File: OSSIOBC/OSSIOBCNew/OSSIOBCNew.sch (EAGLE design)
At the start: 151 parts, among them Q2 NX-3215, U1 PCA9548APWR, U10 MAX6369, U11 OPA4347, U12 TPS73233, U13 SN65HVD11QD, U14 LTC4411, U16 DS3231-L, U17 FM24V02-G, U18 TMP101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

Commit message: New OBC schematic / board file ok
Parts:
- removed C35: 1uF 0805, OSSI:C0805(2012)
- removed U12: TPS73233, OSSI:TPS73233
- added C42: 10uF, LDO Tantal 16V, OSSI:C-TANTAL-A
- added R75, R76, R77: 0, OSSI:R0603(1608)
- added U$1: OSSILOGORECT, OSSI:OSSILOGORECT
- added U15: MCP1700_SOT23, OSSI:MCP1700_SOT23
- C34: value 1uF 0805 -> 10uF, LDO Tantal 16V; device OSSI:C0805(2012) -> OSSI:C-TANTAL-A
- U9: value ADR127BUJZ-REEL7 -> ADR121
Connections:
- new net N$59: C42.-, R75.1
- new net N$62: R76.1, U5.49
- new net N$64: R77.1, U5.50
- net 3.3VOBC: now also C42.+, U15.2; no longer C34.1, R5.2, R72.2, U12.5
- net 3.3VOBC_I2C: now also R5.2, R72.2
- net GND: now also C34.-, R75.2, U15.1; no longer C34.2, C35.2, U12.2
- net MUX_A0: now also R76.2; no longer U5.49
- net MUX_A1: now also R77.2; no longer U5.50
- net N$666: now also C34.+, U15.3; no longer C35.1, U12.1, U12.3
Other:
- note added: "Remove 0 Ohm for SMCLK / ACLK out"
- moved on the sheet: C5

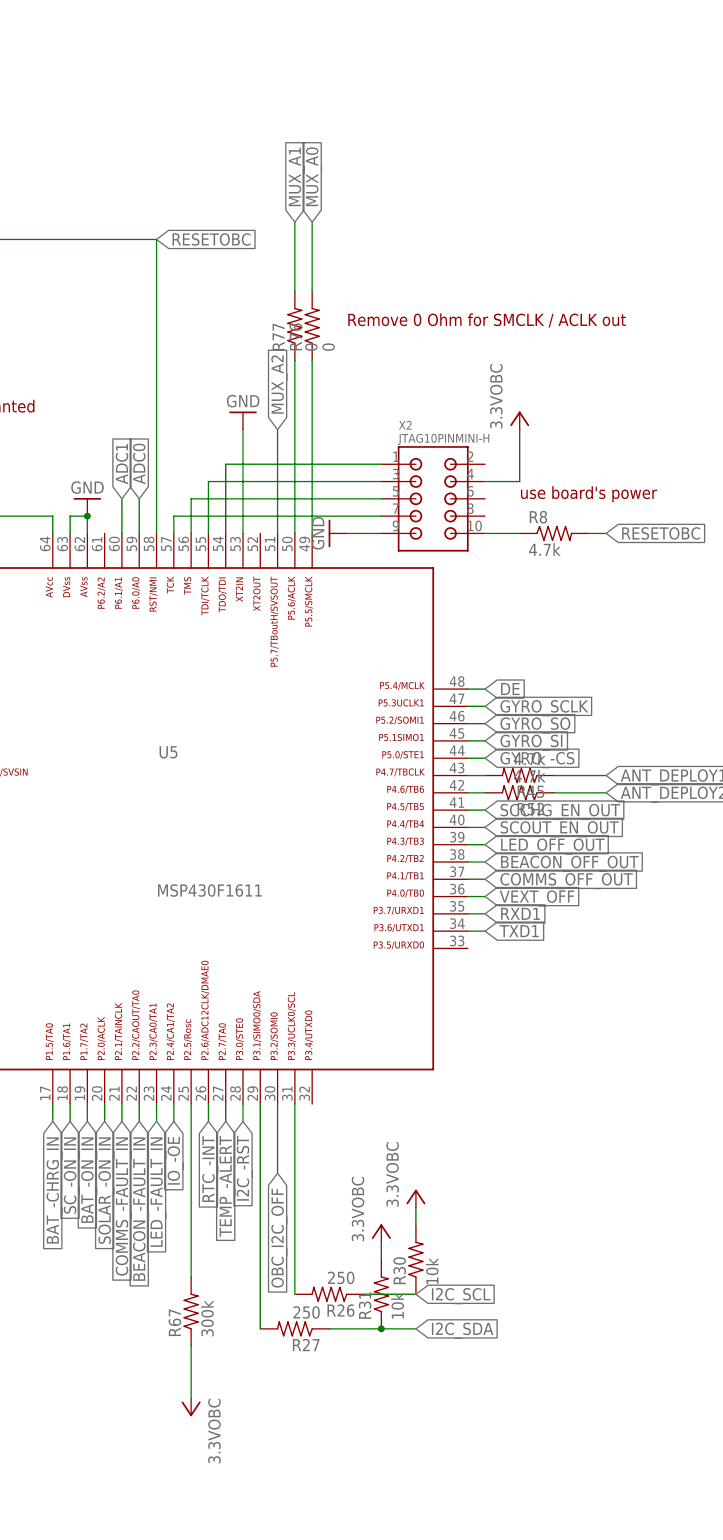
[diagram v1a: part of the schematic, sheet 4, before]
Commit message: OSSI OBC New Gerber file added
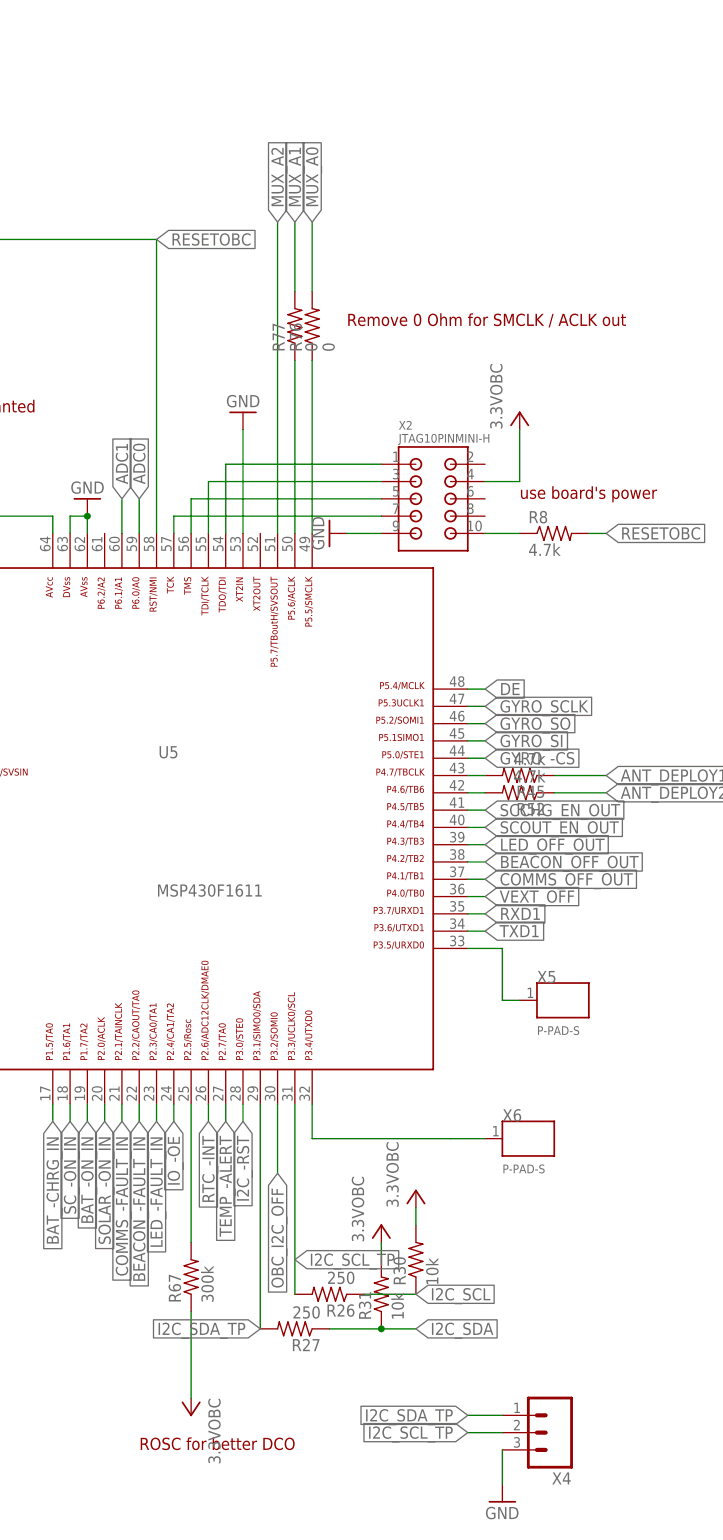
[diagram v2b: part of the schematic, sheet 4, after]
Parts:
- added X4: (no value), OSSI:M03PTH
- added X5, X6: P-PAD-S, OSSI:P-PAD-S
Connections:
- new net I2C_SCL_TP: R26.2, U5.31, X4.2
- new net I2C_SDA_TP: R27.2, U5.29, X4.1
- net GND: now also X4.3
- net N$60: now also U5.33, X5.P$1; no longer R27.2, U5.29
- net N$61: now also U5.32, X6.P$1; no longer R26.2, U5.31
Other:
- note added: "ROSC for better DCO"
- moved on the sheet: R67
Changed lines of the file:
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@@
 <part name="R76" library="OSSI" deviceset="R" device="0603(1608)" value="0"/>
 <part name="R77" library="OSSI" deviceset="R" device="0603(1608)" value="0"/>
+<part name="X4" library="OSSI" deviceset="M03" device="PTH"/>
+<part name="GND81" library="OSSI" deviceset="GND" device=""/>
+<part name="X5" library="OSSI" deviceset="P-PAD" device="-S"/>
+<part name="X6" library="OSSI" deviceset="P-PAD" device="-S"/>
 </parts>
 <sheets>
@@
 <text x="121.92" y="114.3" size="1.778" layer="94">led</text>
 <text x="238.76" y="205.74" size="1.778" layer="94">Remove 0 Ohm for SMCLK / ACLK out</text>
+<text x="208.28" y="40.64" size="1.778" layer="94">ROSC for better DCO</text>
 </plain>
 <instances>
@@
 <instance part="GND74" gate="1" x="114.3" y="88.9"/>
 <instance part="GND70" gate="1" x="223.52" y="193.04" rot="R180"/>
-<instance part="R67" gate="G$1" x="215.9" y="60.96" rot="R90"/>
+<instance part="R67" gate="G$1" x="215.9" y="66.04" rot="R90"/>
 <instance part="3.3VOBC16" gate="G$1" x="215.9" y="48.26" rot="R180"/>
 <instance part="JP1" gate="A" x="129.54" y="99.06"/>
@@
 <instance part="R76" gate="G$1" x="233.68" y="205.74" rot="R90"/>
 <instance part="R77" gate="G$1" x="231.14" y="205.74" rot="R90"/>
+<instance part="X4" gate="G$1" x="269.24" y="43.18" rot="R180"/>
+<instance part="GND81" gate="1" x="261.62" y="33.02"/>
+<instance part="X5" gate="G$1" x="269.24" y="106.68"/>
+<instance part="X6" gate="G$1" x="264.16" y="86.36"/>
 </instances>
 <busses>
@@
 <wire x1="142.24" y1="220.98" x2="142.24" y2="223.52" width="0.1524" layer="91"/>
 </segment>
+<segment>
+<pinref part="X4" gate="G$1" pin="3"/>
+<pinref part="GND81" gate="1" pin="GND"/>
+<wire x1="261.62" y1="40.64" x2="261.62" y2="35.56" width="0.1524" layer="91"/>
+</segment>
 </net>
 <net name="RESETOBC" class="0">
@@
 </segment>
 </net>
-<net name="N$60" class="0">
+<net name="I2C_SDA_TP" class="0">
 <segment>
 <pinref part="U5" gate="G$1" pin="29"/>
 <wire x1="226.06" y1="91.44" x2="226.06" y2="58.42" width="0.1524" layer="91"/>
 <pinref part="R27" gate="G$1" pin="2"/>
+<label x="226.06" y="58.42" size="1.778" layer="95" rot="R180" xref="yes"/>
+</segment>
+<segment>
+<pinref part="X4" gate="G$1" pin="1"/>
+<wire x1="261.62" y1="45.72" x2="256.54" y2="45.72" width="0.1524" layer="91"/>
+<label x="256.54" y="45.72" size="1.778" layer="95" rot="R180" xref="yes"/>
 </segment>
 </net>
-<net name="N$61" class="0">
+<net name="I2C_SCL_TP" class="0">
 <segment>
 <pinref part="U5" gate="G$1" pin="31"/>
 <wire x1="231.14" y1="91.44" x2="231.14" y2="63.5" width="0.1524" layer="91"/>
 <pinref part="R26" gate="G$1" pin="2"/>
+<label x="231.14" y="68.58" size="1.778" layer="95" xref="yes"/>
+</segment>
+<segment>
+<pinref part="X4" gate="G$1" pin="2"/>
+<wire x1="261.62" y1="43.18" x2="256.54" y2="43.18" width="0.1524" layer="91"/>
+<label x="256.54" y="43.18" size="1.778" layer="95" rot="R180" xref="yes"/>
 </segment>
 </net>
@@
 <pinref part="3.3VOBC16" gate="G$1" pin="3.3VOBC"/>
 <pinref part="R67" gate="G$1" pin="1"/>
-<wire x1="215.9" y1="48.26" x2="215.9" y2="55.88" width="0.1524" layer="91"/>
+<wire x1="215.9" y1="48.26" x2="215.9" y2="60.96" width="0.1524" layer="91"/>
 </segment>
 </net>
@@
 <segment>
 <pinref part="U5" gate="G$1" pin="51"/>
-<wire x1="228.6" y1="175.26" x2="228.6" y2="190.5" width="0.1524" layer="91"/>
-<label x="228.6" y="190.5" size="1.778" layer="95" rot="R90" xref="yes"/>
+<wire x1="228.6" y1="175.26" x2="228.6" y2="220.98" width="0.1524" layer="91"/>
+<label x="228.6" y="220.98" size="1.778" layer="95" rot="R90" xref="yes"/>
 </segment>
 </net>
@@
 <pinref part="R67" gate="G$1" pin="2"/>
 <pinref part="U5" gate="G$1" pin="25"/>
-<wire x1="215.9" y1="66.04" x2="215.9" y2="91.44" width="0.1524" layer="91"/>
+<wire x1="215.9" y1="71.12" x2="215.9" y2="91.44" width="0.1524" layer="91"/>
 </segment>
 </net>
@@
 </segment>
 </net>
+<net name="N$60" class="0">
+<segment>
+<pinref part="U5" gate="G$1" pin="33"/>
+<wire x1="256.54" y1="114.3" x2="261.62" y2="114.3" width="0.1524" layer="91"/>
+<wire x1="261.62" y1="114.3" x2="261.62" y2="106.68" width="0.1524" layer="91"/>
+<pinref part="X5" gate="G$1" pin="P$1"/>
+<wire x1="264.16" y1="106.68" x2="261.62" y2="106.68" width="0.1524" layer="91"/>
+</segment>
+</net>
+<net name="N$61" class="0">
+<segment>
+<pinref part="U5" gate="G$1" pin="32"/>
+<wire x1="233.68" y1="91.44" x2="233.68" y2="86.36" width="0.1524" layer="91"/>
+<wire x1="233.68" y1="86.36" x2="254" y2="86.36" width="0.1524" layer="91"/>
+<pinref part="X6" gate="G$1" pin="P$1"/>
+<wire x1="259.08" y1="86.36" x2="254" y2="86.36" width="0.1524" layer="91"/>
+</segment>
+</net>
